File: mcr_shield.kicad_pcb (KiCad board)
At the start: 2 copper layers, 95 x 85 mm, 24 parts, among them J2 MCR_P1_Controls, J3 MCR_System_Coin, J4 MCR_Opt_X_Dial, J5 MCR_P2_Controls, SW1 Game_Selector, SW2 Cabinet_Options, U1 Buck_Regulator, U2 Optocoupler_P1, U3 Optocoupler_Sys, U4 Sync_Buffer, U5 Audio_Amplifier

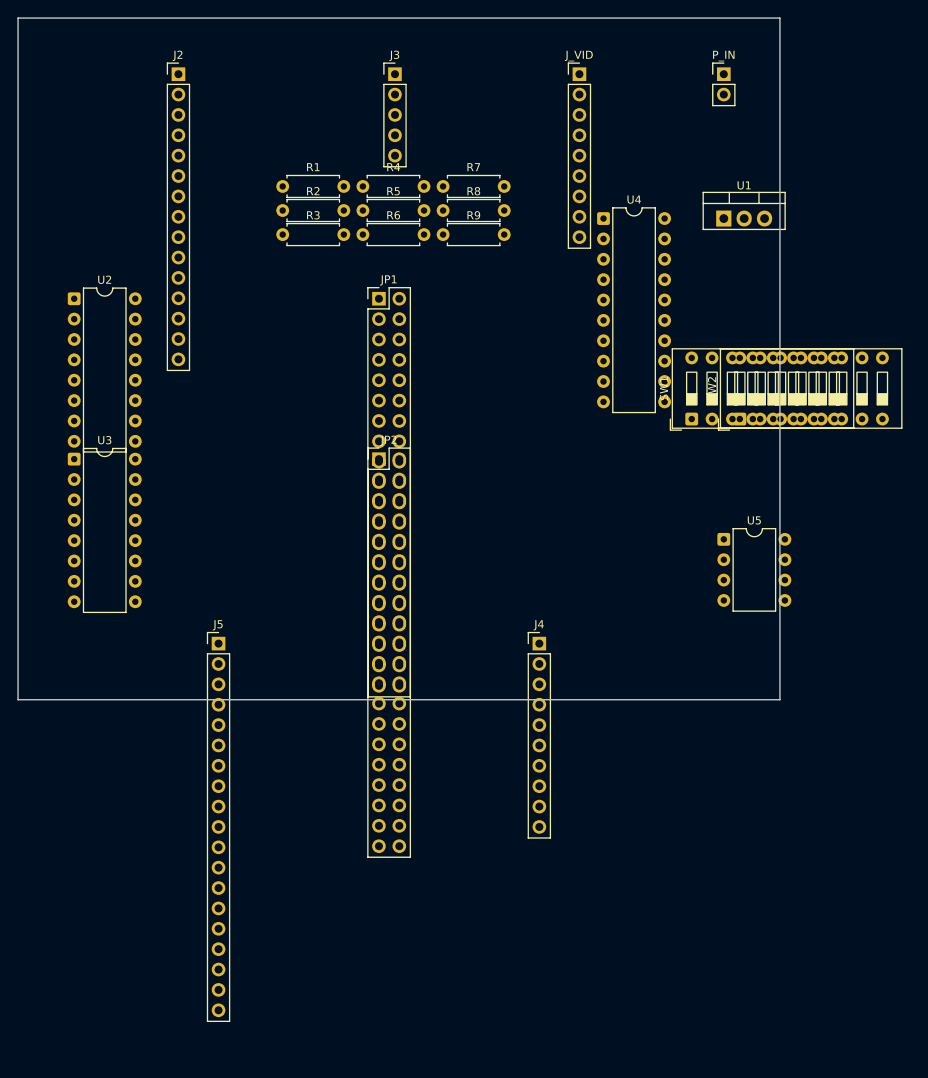
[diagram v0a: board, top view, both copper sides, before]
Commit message: Expand board to 110x90, stack DIPs North/South, and plot thick outlines
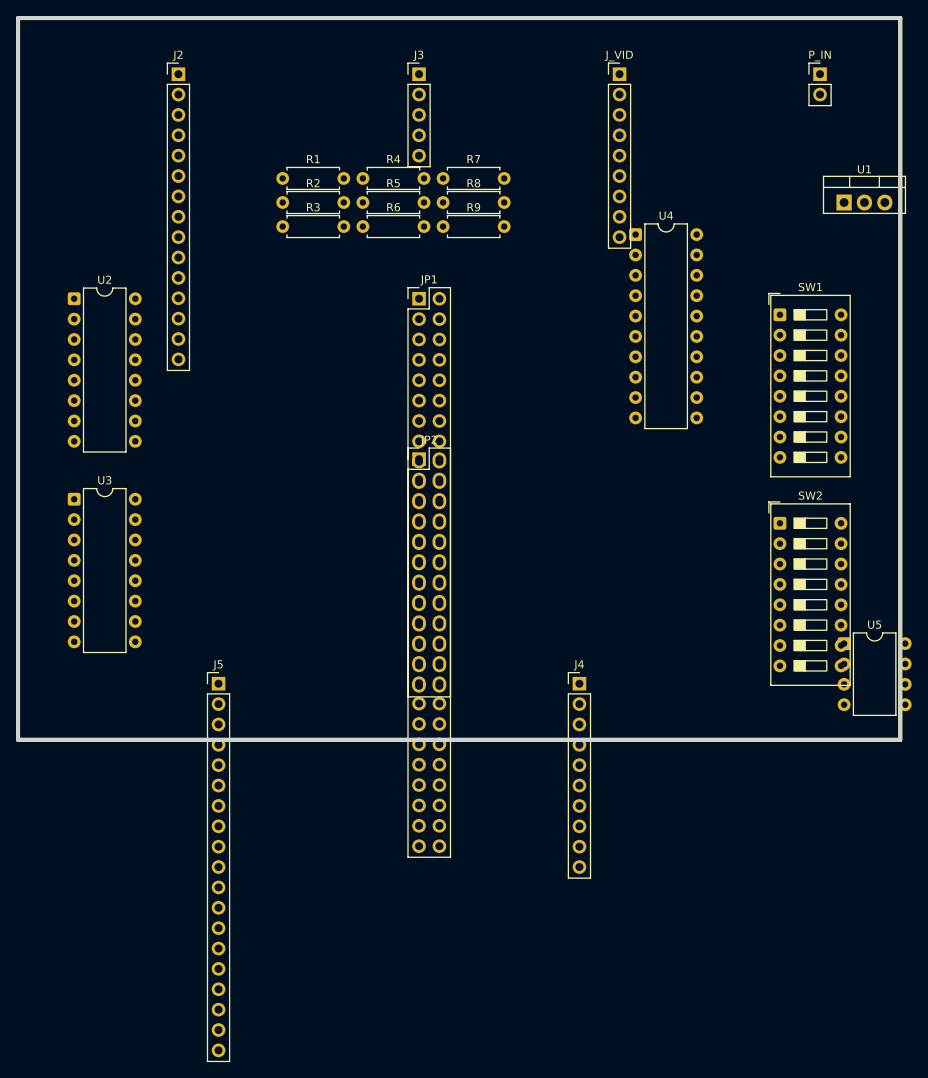
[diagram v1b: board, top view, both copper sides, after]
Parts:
- moved U5 19.8 mm to (108.0, 83.0)
- moved SW1 17.0 mm to (100.0, 42.0), turned to 0 degrees
- moved U1 15.1 mm to (108.0, 28.0)
- moved SW2 13.9 mm to (100.0, 68.0), turned to 0 degrees
- moved P_IN 12.0 mm to (105.0, 12.0)
- moved J4 7.07 mm to (75.0, 88.0)
- moved J5 5.00 mm to (30.0, 88.0)
- moved JP1 5.00 mm to (55.0, 40.0)
- moved JP2 5.00 mm to (55.0, 60.0)
- moved J_VID 5.00 mm to (80.0, 12.0)
- moved U3 5.00 mm to (12.0, 65.0)
- moved U4 4.47 mm to (82.0, 32.0)
- moved J3 3.00 mm to (55.0, 12.0)
- moved R1 1.00 mm to (38.0, 25.0)
- moved R2 1.00 mm to (38.0, 28.0)
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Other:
- board size 95 x 85 mm -> 110 x 90 mm
